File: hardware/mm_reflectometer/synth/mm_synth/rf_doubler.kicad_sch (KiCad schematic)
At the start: 30 parts, among them U501 MAAM-011101, U502 XX1000-QT, U503 ADMV8432

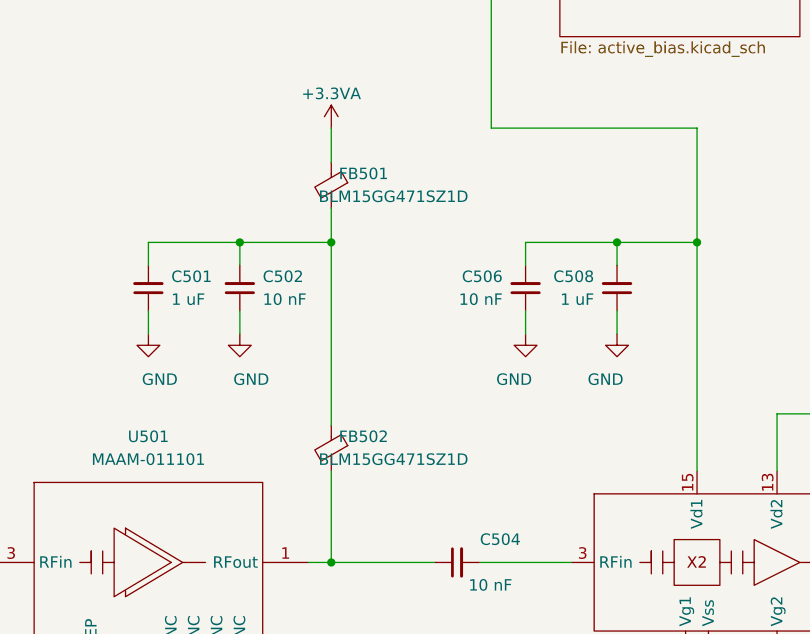
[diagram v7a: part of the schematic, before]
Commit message: added usb PD sink to synth
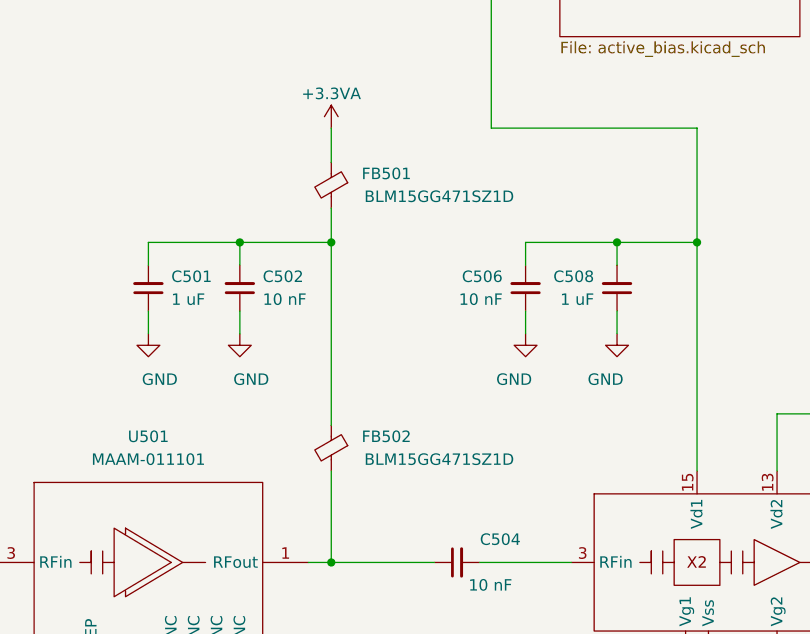
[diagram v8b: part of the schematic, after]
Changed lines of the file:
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@@
   (symbol (lib_id "Device:FerriteBead_Small") (at 91.44 49.53 0) (mirror y) (unit 1)
     (in_bom yes) (on_board yes)
-    (property "Reference" "FB501" (id 0) (at 97.79 48.26 0)
+    (property "Reference" "FB501" (id 0) (at 100.33 48.26 0)
       (effects (font (size 1.27 1.27)) (justify left))
     )
-    (property "Value" "BLM15GG471SZ1D" (id 1) (at 106.68 50.8 0)
+    (property "Value" "BLM15GG471SZ1D" (id 1) (at 111.76 50.8 0)
       (effects (font (size 1.27 1.27)) (justify left))
     )
@@
   (symbol (lib_id "Device:FerriteBead_Small") (at 91.44 78.74 0) (mirror y) (unit 1)
     (in_bom yes) (on_board yes)
-    (property "Reference" "FB502" (id 0) (at 97.79 77.47 0)
+    (property "Reference" "FB502" (id 0) (at 100.33 77.47 0)
       (effects (font (size 1.27 1.27)) (justify left))
     )
-    (property "Value" "BLM15GG471SZ1D" (id 1) (at 106.68 80.01 0)
+    (property "Value" "BLM15GG471SZ1D" (id 1) (at 111.76 80.01 0)
       (effects (font (size 1.27 1.27)) (justify left))
     )
